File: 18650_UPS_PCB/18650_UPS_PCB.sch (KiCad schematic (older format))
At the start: 50 parts, among them J1 USB_B_Micro, J2 Conn_02x04_Odd_Even, J3 USB_A, SW2 ALPSALPINE_SKRHADE011, SW3 SW_SPDT, SW4 SW_SPDT, SW5 SW_SPDT, U1 STLINK-V3MINI, U10 LR9102G-xx, U11 MP2667, U2 INA260, U5 ME2188Cxx, U6 XC9236Axx, U8 SSD1306_128_32, U9 STM32F030F4Px

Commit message: reworked schematic with new components
5V Boost missing
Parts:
- removed C14: 100 nF, Capacitor_SMD:C_0603_1608Metric, symbol Device:C_Small
- removed C15, C16: 200 nF, Capacitor_SMD:C_0603_1608Metric, symbol Device:C_Small
- removed C17: 4.7 uF, Capacitor_SMD:C_0603_1608Metric, symbol Device:C_Small
- removed C18: 10 nF, Capacitor_SMD:C_0603_1608Metric, symbol Device:C_Small
- removed C19: 1 uF, Capacitor_SMD:C_0603_1608Metric, symbol Device:C_Small
- removed C4: 4.7 uF, Capacitor_SMD:C_0805_2012Metric, symbol Device:C_Small
- removed C5, C9: 10 uF, Capacitor_SMD:C_0805_2012Metric, symbol Device:C_Small
- removed C7: 100 uF, Capacitor_SMD:CP_Elec_5x5.4, symbol Device:CP_Small
- removed D2: WS2812B, LED_SMD:LED_WS2812B_PLCC4_5.0x5.0mm_P3.2mm, symbol LED:WS2812B
- removed J2: Conn_02x04_Odd_Even, Connector_PinSocket_2.54mm:PinSocket_2x04_P2.54mm_Vertical_SMD, symbol Connector_Generic:Conn_02x04_Odd_Even
- removed L1: 22 uH, Inductor_SMD:L_Bourns-SRN6028, symbol Device:L_Small
- removed L2: 1.5 uH, Inductor_SMD:L_Taiyo-Yuden_MD-4040, symbol Device:L_Small
- removed R12, R13, R17, R6, R7: 10 kOhm, Resistor_SMD:R_0603_1608Metric, symbol Device:R_Small
- removed SW2: ALPSALPINE_SKRHADE011, CUSTOM_FOOTPRINTS:SKRHADE011, symbol CUSTOM_PARTS:ALPSALPINE_SKRHADE011
- removed SW3, SW4, SW5: SW_SPDT, Button_Switch_SMD:SW_SPDT_PCM12, symbol Switch:SW_SPDT
- removed U5: ME2188Cxx, Package_TO_SOT_SMD:SOT-23-5, symbol CUSTOM_PARTS:ME2188Cxx
- removed U6: XC9236Axx, Package_TO_SOT_SMD:SOT-23-5, symbol CUSTOM_PARTS:XC9236Axx
- removed U8: SSD1306_128_32, Connector_PinHeader_2.54mm:PinHeader_1x04_P2.54mm_Vertical_SMD_Pin1Left, symbol CUSTOM_PARTS:SSD1306_128_32
- removed U9: STM32F030F4Px, Package_SO:TSSOP-20_4.4x6.5mm_P0.65mm, symbol MCU_ST_STM32F0:STM32F030F4Px
- added C? (x2): 1 uF, Capacitor_SMD:C_0603_1608Metric, symbol Device:C_Small
- added J? (x4): Conn_01x02, Connector_PinSocket_2.54mm:PinSocket_1x02_P2.54mm_Vertical, symbol Connector_Generic:Conn_01x02
- added JP?: EA_ADR, Jumper:SolderJumper-3_P1.3mm_Open_RoundedPad1.0x1.5mm, symbol Jumper:SolderJumper_3_Open
- added S?: TM-2027, CUSTOM_FOOTPRINTS:TM-2027, symbol CUSTOM_PARTS:TM-2027
- added SW?: SW_DIP_x02, CUSTOM_FOOTPRINTS:TS6637TP-4P, symbol Switch:SW_DIP_x02
- added U?: STM32L151RCTx, Package_QFP:LQFP-64_10x10mm_P0.5mm, symbol MCU_ST_STM32L1:STM32L151RCTx
- added U?: EA_DOGS164N-A, CUSTOM_FOOTPRINTS:EA_DOGS164N-A, symbol CUSTOM_PARTS:EA_DOGS164N-A
- JP1: value SolderJumper_3_Open -> INA_ADR_0
- JP2: value SolderJumper_3_Open -> INA_ADR_1
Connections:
- net labels added: EA_RST, INA-ALERT, MP-INT, TM-A, TM-B, TM-C, TM-Center, TM-D
- net labels removed: +3.3VA, BoostCE, BuckCE, INT, LDOCE, PA0, PA1, PA4, PA5, PA6, PA7, PB1, PF0, PF1
- wire segments 235 -> 157
- no-connect marks 13 -> 12
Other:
- note added: "Control"
- note added: "LCD Textdisplay"
- note added: "TPS61032 -> Symbol"
- note removed: "3V3 Buck"
- note removed: "5V Boost"
- note removed: "MCU"
- note removed: "OLED & Control"
- note removed: "Regulator switches"
- note removed: "WS2812E"
- moved on the sheet: C1, C6, C8, H1, H2, H3, H4, JP1, JP2, R1, U1, U10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

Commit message: schematic done
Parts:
- added C?: 10 uF, symbol Device:C_Small
- added C?: 2.2 uF, symbol Device:C_Small
- added C?: 220 uF, symbol Device:CP1_Small
- added C? (x5): 100 nF, Capacitor_SMD:C_0603_1608Metric, symbol Device:C_Small
- added C?: 4.7 uF, Capacitor_SMD:C_0603_1608Metric, symbol Device:C_Small
- added C?: 1 uF, Capacitor_SMD:C_0603_1608Metric, symbol Device:C_Small
- added C?: 0.1 uF, Capacitor_SMD:C_0603_1608Metric, symbol Device:C_Small
- added JP?: TPS_LBI, Jumper:SolderJumper-3_P1.3mm_Open_RoundedPad1.0x1.5mm, symbol Jumper:SolderJumper_3_Open
- added L?: 6.8 uH, symbol Device:L_Small
- added R?: 10 kOhm, Resistor_SMD:R_0603_1608Metric, symbol Device:R_Small
- added U?: TPS61032, Package_SO:HTSSOP-16-1EP_4.4x5mm_P0.65mm_EP3.4x5mm, symbol CUSTOM_PARTS:TPS61032
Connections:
- net labels added: EA-RST, TPS-EN, TPS-SYNC
- net labels removed: EA_RST
- wire segments 157 -> 264
- no-connect marks 12 -> 50
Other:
- note added: "5V Boost"
- note removed: "TPS61032 -> Symbol"
- moved on the sheet: U?

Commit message: savepoint before messing up pcbnew
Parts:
- added C?: 100 nF, Capacitor_SMD:C_0603_1608Metric, symbol Device:C_Small
- C13, C4: renamed from C?; footprint (none) -> Capacitor_SMD:C_0603_1608Metric
- C15: renamed from C?; footprint (none) -> Capacitor_Tantalum_SMD:CP_EIA-7343-43_Kemet-X_Pad2.25x2.55mm_HandSolder
- L1: renamed from L?; footprint (none) -> Inductor_SMD:L_10.4x10.4_H4.8
- gave numbers to parts that had none: 22
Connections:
- wire segments 264 -> 269
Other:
- note added: "MCU"
- moved on the sheet: C12, C14, C16, C17, C18, C5, C7, C9, R2, U5

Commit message: all parts on pcb
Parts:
- removed J3: USB_A, Connector_USB:USB_A_CNCTech_1001-011-01101_Horizontal, symbol Connector:USB_A
- removed U3: EA_DOGS164N-A, CUSTOM_FOOTPRINTS:EA_DOGS164N-A, symbol CUSTOM_PARTS:EA_DOGS164N-A
- added U3: EA_DOGS104N-A, CUSTOM_FOOTPRINTS:EA_DOGS104N-A, symbol CUSTOM_PARTS:EA_DOGS104N-A
- gave numbers to parts that had none: 1
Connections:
- wire segments 269 -> 267
- no-connect marks 50 -> 47
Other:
- note removed: "5V USB Out"
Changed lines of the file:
@@
 Text Notes 5550 900  0    50   ~ 0
 3V3 LDO for onboard
-$Comp
-L Connector:USB_A J3
-U 1 1 60D1113B
-P 4450 9150
-F 0 "J3" H 4507 9617 50  0000 C CNN
-F 1 "USB_A" H 4507 9526 50  0000 C CNN
-F 2 "Connector_USB:USB_A_CNCTech_1001-011-01101_Horizontal" H 4600 9100 50  0001 C CNN
-F 3 " ~" H 4600 9100 50  0001 C CNN
-	1    4450 9150
-	1    0    0    -1
-$EndComp
-Wire Wire Line
-	4450 9650 4450 9550
-NoConn ~ 4350 9550
-NoConn ~ 4750 9250
-NoConn ~ 4750 9150
-$Comp
-L power:+5V #PWR0102
-U 1 1 60D43744
-P 4850 8850
-AR Path="/60D43744" Ref="#PWR0102"  Part="1"
-AR Path="/60952D5B/60D43744" Ref="#PWR?"  Part="1"
-F 0 "#PWR0102" H 4850 8700 50  0001 C CNN
-F 1 "+5V" H 4865 9023 50  0000 C CNN
-F 2 "" H 4850 8850 50  0001 C CNN
-F 3 "" H 4850 8850 50  0001 C CNN
-	1    4850 8850
-	1    0    0    -1
-$EndComp
-Wire Wire Line
-	4750 8950 4850 8950
-Wire Wire Line
-	4850 8950 4850 8850
-Wire Notes Line
-	3750 8250 5750 8250
-Text Notes 3900 8450 0    50   ~ 0
-5V USB Out
 Wire Wire Line
 	7600 1300 7600 1200
@@
 	1    0    0    -1
 $EndComp
-$Comp
-L power:GND #PWR0132
-U 1 1 61ADEE57
-P 4450 9650
-F 0 "#PWR0132" H 4450 9400 50  0001 C CNN
-F 1 "GND" H 4455 9477 50  0000 C CNN
-F 2 "" H 4450 9650 50  0001 C CNN
-F 3 "" H 4450 9650 50  0001 C CNN
-	1    4450 9650
-	1    0    0    -1
-$EndComp
-Wire Notes Line
-	3750 8250 3750 10050
-Wire Notes Line
-	3750 10050 5750 10050
-Wire Notes Line
-	5750 8250 5750 10050
 Wire Notes Line
 	6050 10150 8050 10150
@@
 F 3 "http://www.st.com/st-web-ui/static/active/en/resource/technical/document/datasheet/DM00048356.pdf" H 12300 6200 50  0001 C CNN
 	1    12300 6200
-	1    0    0    -1
-$EndComp
-$Comp
-L CUSTOM_PARTS:EA_DOGS164N-A U3
-U 1 1 6134EF70
-P 1750 8450
-F 0 "U3" H 1900 8265 50  0000 C CNN
-F 1 "EA_DOGS164N-A" H 1900 8174 50  0000 C CNN
-F 2 "CUSTOM_FOOTPRINTS:EA_DOGS164N-A" H 2550 8350 50  0001 C CNN
-F 3 "" H 1600 8200 50  0001 C CNN
-	1    1750 8450
 	1    0    0    -1
 $EndComp
@@
 	8700 8750 8700 3250
 $Comp
-L Device:C_Small C?
+L Device:C_Small C19
 U 1 1 61875D52
 P 9750 1600
-F 0 "C?" H 9450 1650 50  0000 L CNN
+F 0 "C19" H 9450 1650 50  0000 L CNN
 F 1 "100 nF" H 9350 1550 50  0000 L CNN
 F 2 "Capacitor_SMD:C_0603_1608Metric" H 9750 1600 50  0001 C CNN
@@
 Wire Wire Line
 	9750 1450 9900 1450
+$Comp
+L power:VBUS #PWR01
+U 1 1 6191A448
+P 1700 1150
+F 0 "#PWR01" H 1700 1000 50  0001 C CNN
+F 1 "VBUS" H 1715 1323 50  0000 C CNN
+F 2 "" H 1700 1150 50  0001 C CNN
+F 3 "" H 1700 1150 50  0001 C CNN
+	1    1700 1150
+	1    0    0    -1
+$EndComp
+Wire Wire Line
+	1700 1250 1700 1150
+$Comp
+L CUSTOM_PARTS:EA_DOGS104N-A U3
+U 1 1 610AB50A
+P 1750 8450
+F 0 "U3" H 1900 8265 50  0000 C CNN
+F 1 "EA_DOGS104N-A" H 1900 8174 50  0000 C CNN
+F 2 "CUSTOM_FOOTPRINTS:EA_DOGS104N-A" H 2550 8350 50  0001 C CNN
+F 3 "" H 1600 8200 50  0001 C CNN
+	1    1750 8450
+	1    0    0    -1
+$EndComp
 $EndSCHEMATC

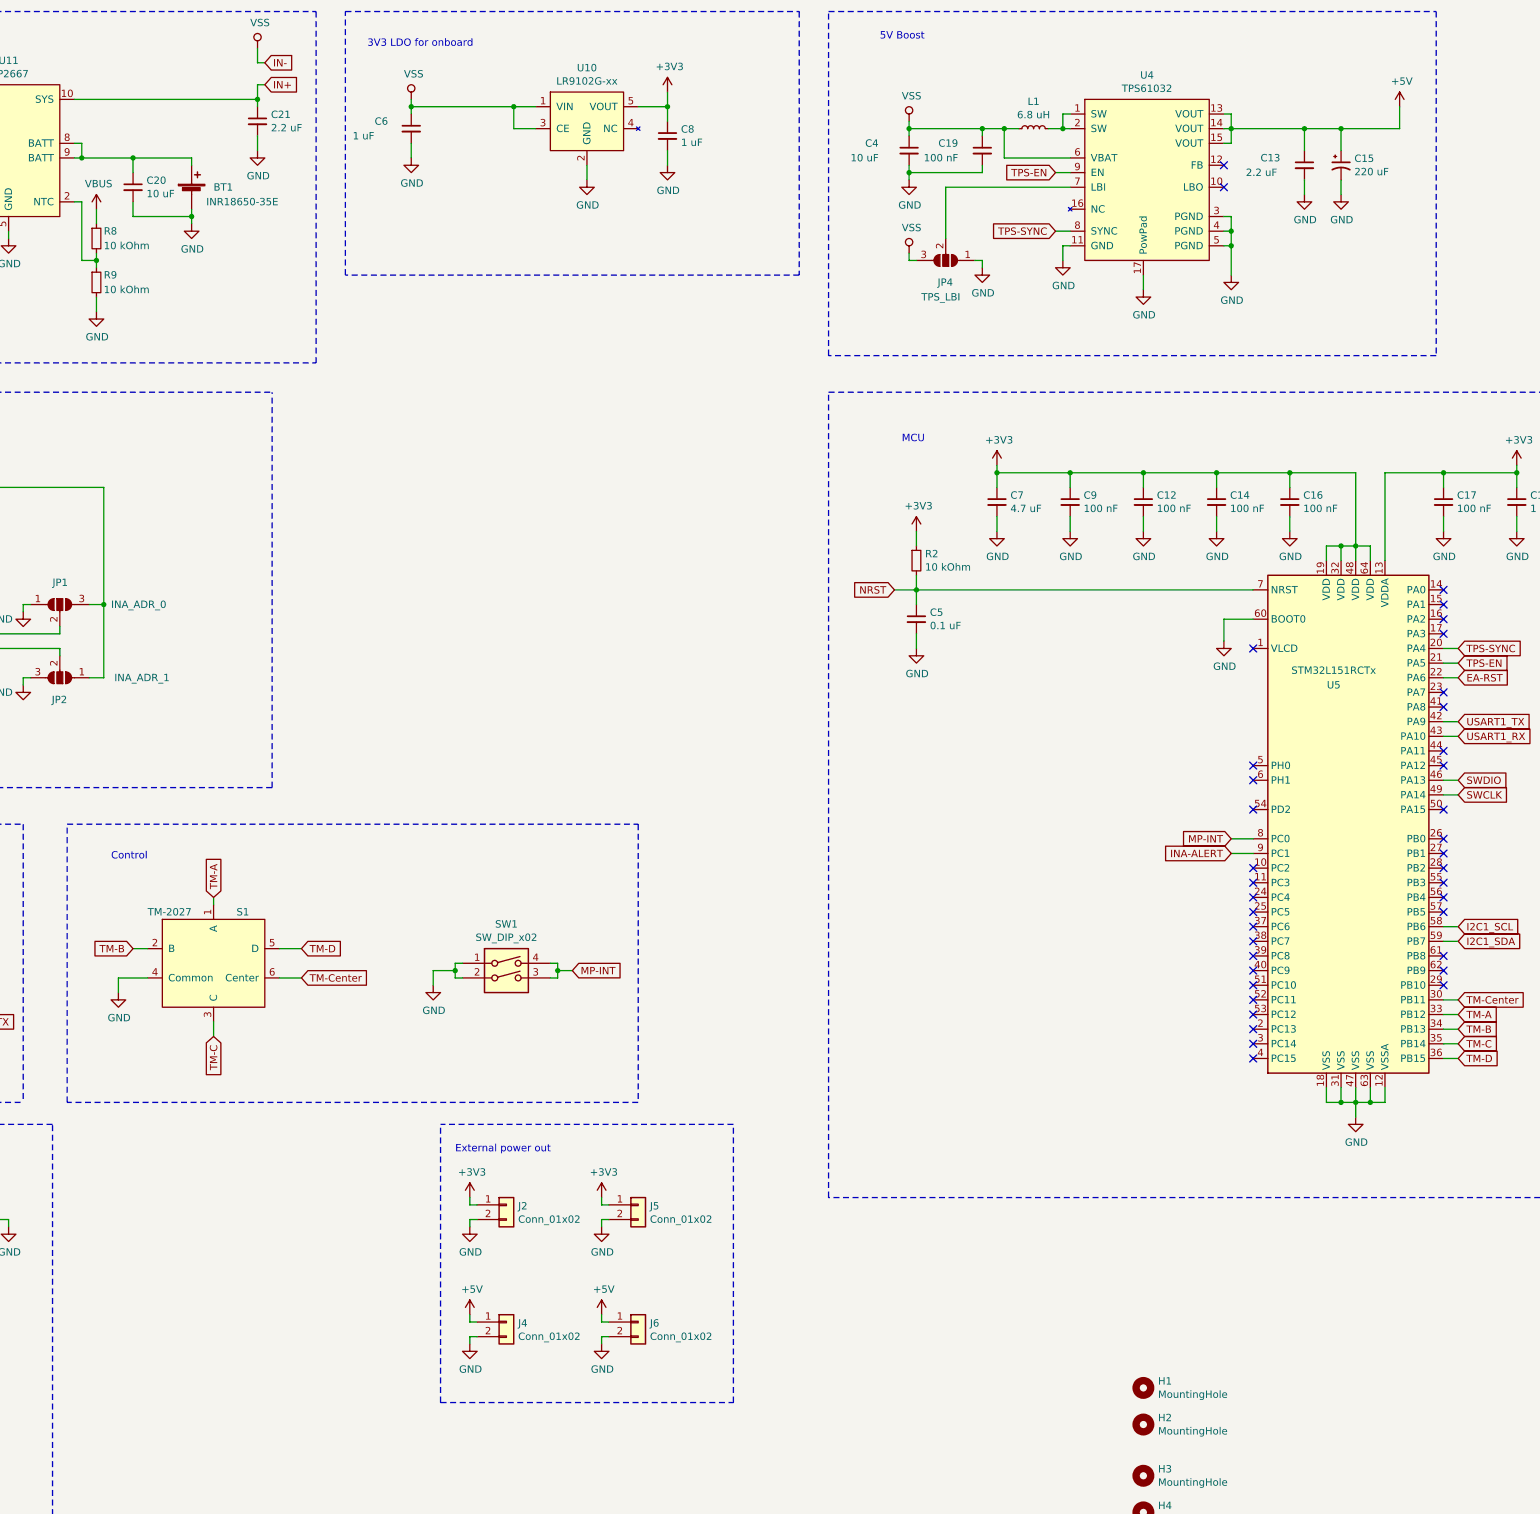
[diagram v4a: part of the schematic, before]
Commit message: placed all components
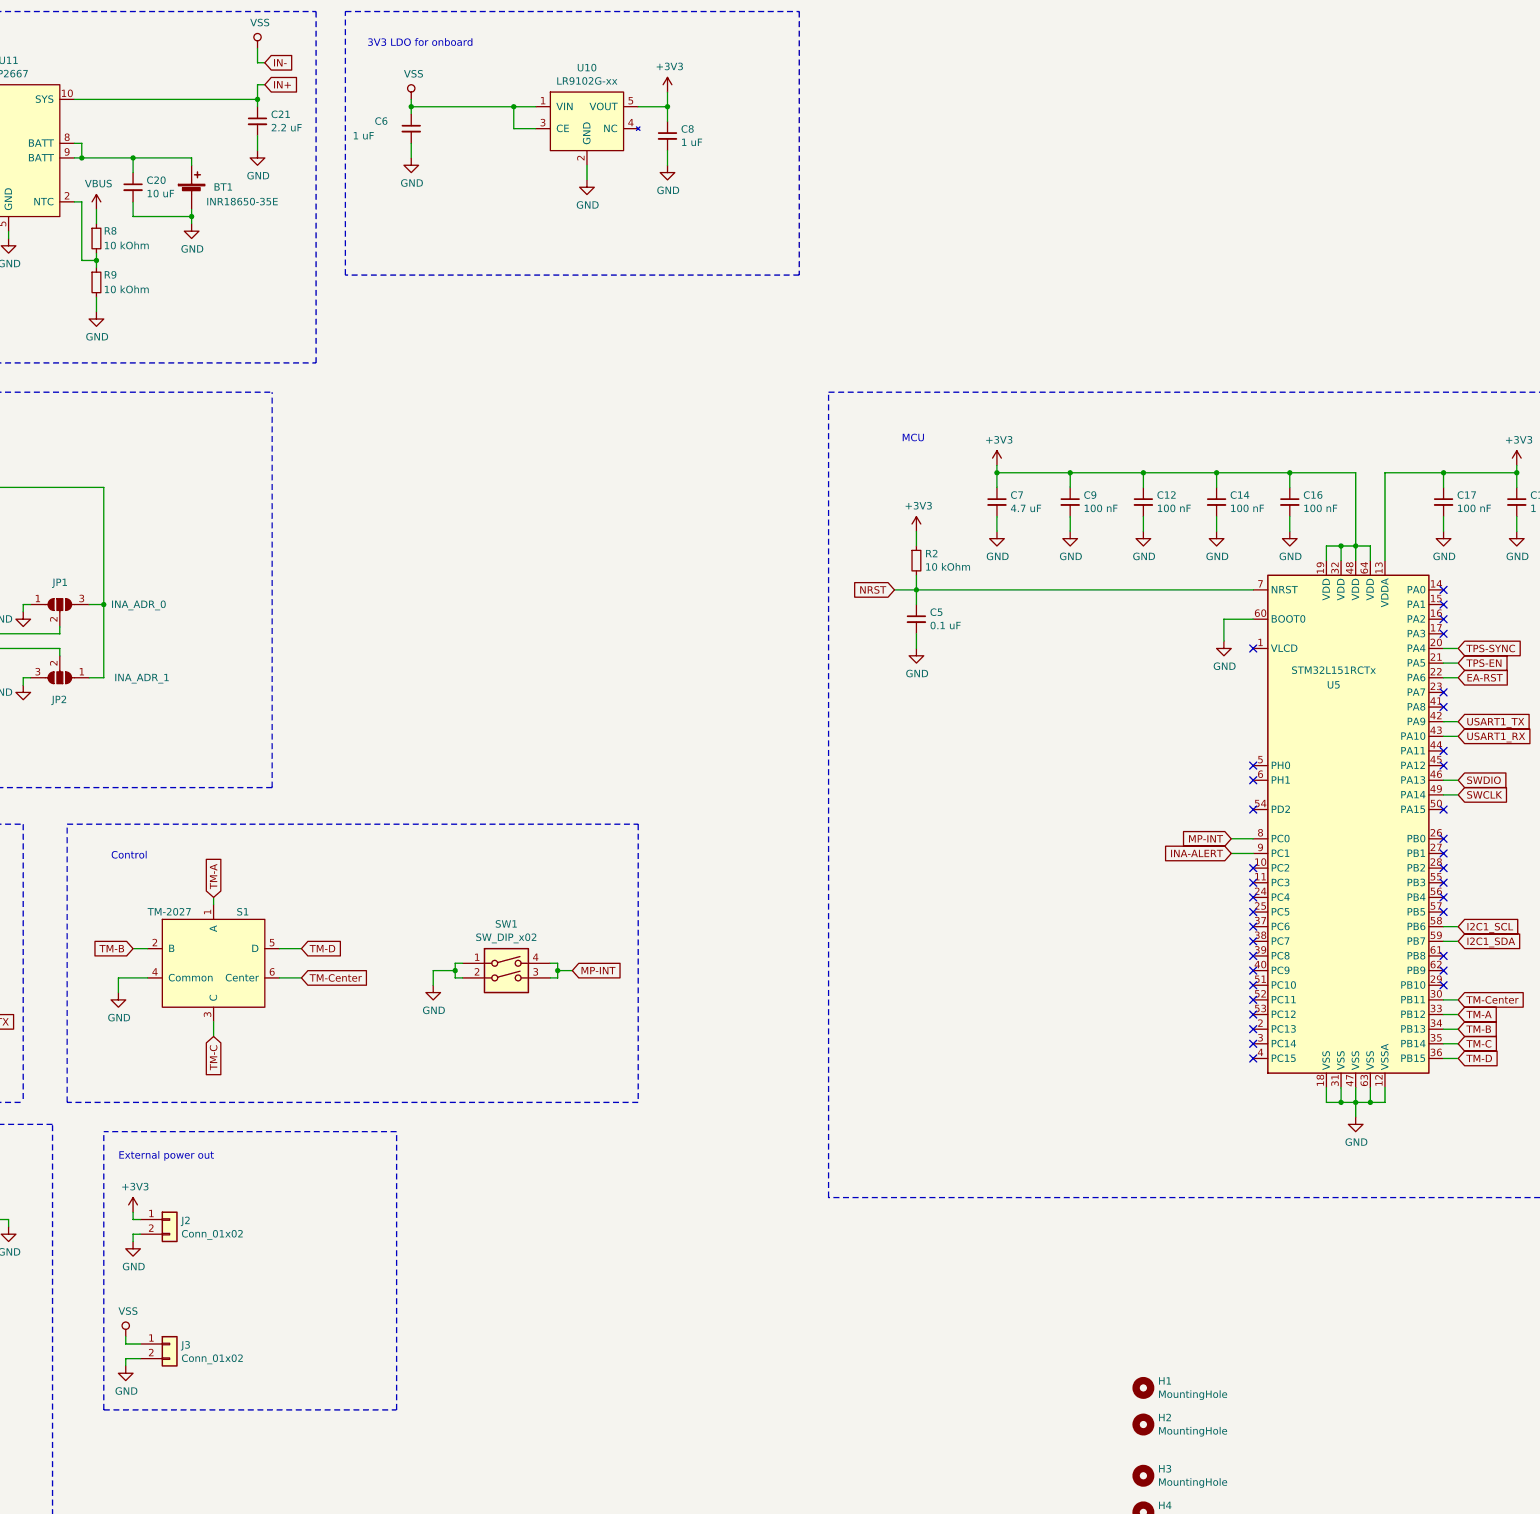
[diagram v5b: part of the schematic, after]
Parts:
- removed C13: 2.2 uF, Capacitor_SMD:C_0603_1608Metric, symbol Device:C_Small
- removed C15: 220 uF, Capacitor_Tantalum_SMD:CP_EIA-7343-43_Kemet-X_Pad2.25x2.55mm_HandSolder, symbol Device:CP1_Small
- removed C19: 100 nF, Capacitor_SMD:C_0603_1608Metric, symbol Device:C_Small
- removed C4: 10 uF, Capacitor_SMD:C_0603_1608Metric, symbol Device:C_Small
- removed J4, J5, J6: Conn_01x02, Connector_PinSocket_2.54mm:PinSocket_1x02_P2.54mm_Vertical, symbol Connector_Generic:Conn_01x02
- removed JP4: TPS_LBI, Jumper:SolderJumper-3_P1.3mm_Open_RoundedPad1.0x1.5mm, symbol Jumper:SolderJumper_3_Open
- removed L1: 6.8 uH, Inductor_SMD:L_10.4x10.4_H4.8, symbol Device:L_Small
- removed U4: TPS61032, Package_SO:HTSSOP-16-1EP_4.4x5mm_P0.65mm_EP3.4x5mm, symbol CUSTOM_PARTS:TPS61032
- added J3: Conn_01x02, Connector_PinSocket_2.54mm:PinSocket_1x02_P2.54mm_Vertical, symbol Connector_Generic:Conn_01x02
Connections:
- net GND: now also J3.2 (Pin_2)
- net VSS: now also J3.1 (Pin_1)
- no-connect marks 47 -> 45
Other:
- note removed: "5V Boost"
- moved on the sheet: J2

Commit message: changed to ina 237/239
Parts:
- removed U2: INA260, Package_SO:TSSOP-16_4.4x5mm_P0.65mm, symbol Sensor:INA260
- added R3, R4, R5: 10 kOhm, Resistor_SMD:R_0603_1608Metric, symbol Device:R_Small
- added U2: INA237, Package_SO:VSSOP-10_3x3mm_P0.5mm, symbol CUSTOM_PARTS:INA237
- R1: value 10 kOhm -> 0.01 Ohm; footprint Resistor_SMD:R_0603_1608Metric -> Resistor_SMD:R_0805_2012Metric
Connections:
- net +3V3: now also R3.1, R4.1, R5.1, U2.6 (VS); no longer R1.1
- net GND: now also U2.7 (GND)
- net I2C1_SCL: now also R4.2, U2.5 (SCL)
- net I2C1_SDA: now also R5.2, U2.4 (SDA)
- net IN+: now also R1.1, U2.10 (IN+)
- net INA-ALERT: now also R3.2, U2.3 (ALERT); no longer R1.2
- net VSS: now also R1.2, U2.8 (VBUS), U2.9 (IN-)
- net at JP2.2 (C): now also U2.1 (A1)
- net at JP1.2 (C): now also U2.2 (A0)
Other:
- moved on the sheet: C12, C14, C16, C17, C18, C5, C7, C9, JP1, JP2, R2, U5
